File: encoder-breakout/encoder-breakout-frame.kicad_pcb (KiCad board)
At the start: 2 copper layers, 76 x 62.2 mm, 60 parts, among them J1 Conn_01x06_Female, U1 AEDR-8300

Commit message: Replace tooling holes with dual sided version
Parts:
- removed the REF** at (205.0, 112.0)
- removed the REF** at (205.0, 132.0)
- removed the REF** at (135.0, 142.0)
- added REF**: Tooling hole 4mm_4.04mm_paste, Jitter_Footprints:Tooling_hole_4mm_4.04mm_paste_dual_sided, F.Cu at (205.0, 112.0)
- added REF**: Tooling hole 4mm_4.04mm_paste, Jitter_Footprints:Tooling_hole_4mm_4.04mm_paste_dual_sided, F.Cu at (205.0, 132.0)
- added REF**: Tooling hole 4mm_4.04mm_paste, Jitter_Footprints:Tooling_hole_4mm_4.04mm_paste_dual_sided, F.Cu at (135.0, 142.0)
- REF**: value Tooling hole 4mm_4.04mm_paste -> Tooling hole 4mm_4.04mm_paste_dual_sided; footprint Jitter_Footprints:Tooling_hole_4mm_4.04mm_paste -> Jitter_Footprints:Tooling_hole_4mm_4.04mm_paste_dual_sided
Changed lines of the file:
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@@
-(kicad_pcb (version 20171130) (host pcbnew "(5.1.4-0-10_14)")
+(kicad_pcb (version 20171130) (host pcbnew 5.1.4-e60b266~84~ubuntu16.04.1)
   (general
     (thickness 1.6)
@@
       (outputformat 1)
       (mirror false)
-      (drillshape 1)
+      (drillshape 0)
       (scaleselection 1)
-      (outputdirectory ""))
+      (outputdirectory "gerber__76x63/"))
   )
   (net 0 "")
@@
     (add_net "Net-(R2-Pad2)")
   )
+  (module Jitter_Footprints:Tooling_hole_4mm_4.04mm_paste_dual_sided locked (layer F.Cu)
+    (at 205 112)
+    (fp_text reference REF** (at -4.8 -1.5) (layer F.SilkS) hide
+      (effects (font (size 1 1) (thickness 0.15)))
+    )
+    (fp_text value "Tooling hole 4mm_4.04mm_paste" (at 0 -3.2) (layer F.Fab) hide
+      (effects (font (size 1 1) (thickness 0.15)))
+    )
+    (pad "" np_thru_hole circle (at 0 0) (size 4 4) (drill 4) (layers *.Cu *.Paste *.Mask)
+      (solder_paste_margin 0.04))
+  )
+  (module Jitter_Footprints:Tooling_hole_4mm_4.04mm_paste_dual_sided locked (layer F.Cu)
+    (at 205 132)
+    (fp_text reference REF** (at -4.8 -1.5) (layer F.SilkS) hide
+      (effects (font (size 1 1) (thickness 0.15)))
+    )
+    (fp_text value "Tooling hole 4mm_4.04mm_paste" (at 0 -3.2) (layer F.Fab) hide
+      (effects (font (size 1 1) (thickness 0.15)))
+    )
+    (pad "" np_thru_hole circle (at 0 0) (size 4 4) (drill 4) (layers *.Cu *.Paste *.Mask)
+      (solder_paste_margin 0.04))
+  )
+  (module Jitter_Footprints:Tooling_hole_4mm_4.04mm_paste_dual_sided locked (layer F.Cu)
+    (at 135 142)
+    (fp_text reference REF** (at -4.8 -1.5) (layer F.SilkS) hide
+      (effects (font (size 1 1) (thickness 0.15)))
+    )
+    (fp_text value "Tooling hole 4mm_4.04mm_paste" (at 0 -3.2) (layer F.Fab) hide
+      (effects (font (size 1 1) (thickness 0.15)))
+    )
+    (pad "" np_thru_hole circle (at 0 0) (size 4 4) (drill 4) (layers *.Cu *.Paste *.Mask)
+      (solder_paste_margin 0.04))
+  )
+  (module Jitter_Footprints:Tooling_hole_4mm_4.04mm_paste_dual_sided locked (layer F.Cu)
+    (at 135 102)
+    (fp_text reference REF** (at -4.8 -1.5) (layer F.SilkS) hide
+      (effects (font (size 1 1) (thickness 0.15)))
+    )
+    (fp_text value "Tooling hole 4mm_4.04mm_paste_dual_sided" (at 0 -3.2) (layer F.Fab) hide
+      (effects (font (size 1 1) (thickness 0.15)))
+    )
+    (pad "" np_thru_hole circle (at 0 0) (size 4 4) (drill 4) (layers *.Cu *.Paste *.Mask)
+      (solder_paste_margin 0.04))
+  )
   (module Jitter_Footprints:MouseBite_3.7mmx2.2mm (layer F.Cu)
     (at 173 122.2 90)
@@
     (pad "" np_thru_hole circle (at 0.25 0.5 180) (size 0.5 0.5) (drill 0.5) (layers *.Cu *.Mask))
   )
-  (module Jitter_Footprints:Tooling_hole_4mm_4.04mm_paste locked (layer F.Cu)
-    (at 205 112)
-    (fp_text reference REF** (at -4.8 -1.5) (layer F.SilkS) hide
-      (effects (font (size 1 1) (thickness 0.15)))
-    )
-    (fp_text value "Tooling hole 4mm_4.04mm_paste" (at 0 -3.2) (layer F.Fab) hide
-      (effects (font (size 1 1) (thickness 0.15)))
-    )
-    (pad "" np_thru_hole circle (at 0 0) (size 4 4) (drill 4) (layers *.Cu *.Mask F.Paste)
-      (solder_paste_margin 0.04))
-  )
-  (module Jitter_Footprints:Tooling_hole_4mm_4.04mm_paste locked (layer F.Cu)
-    (at 205 132)
-    (fp_text reference REF** (at -4.8 -1.5) (layer F.SilkS) hide
-      (effects (font (size 1 1) (thickness 0.15)))
-    )
-    (fp_text value "Tooling hole 4mm_4.04mm_paste" (at 0 -3.2) (layer F.Fab) hide
-      (effects (font (size 1 1) (thickness 0.15)))
-    )
-    (pad "" np_thru_hole circle (at 0 0) (size 4 4) (drill 4) (layers *.Cu *.Mask F.Paste)
-      (solder_paste_margin 0.04))
-  )
-  (module Jitter_Footprints:Tooling_hole_4mm_4.04mm_paste locked (layer F.Cu)
-    (at 135 142)
-    (fp_text reference REF** (at -4.8 -1.5) (layer F.SilkS) hide
-      (effects (font (size 1 1) (thickness 0.15)))
-    )
-    (fp_text value "Tooling hole 4mm_4.04mm_paste" (at 0 -3.2) (layer F.Fab) hide
-      (effects (font (size 1 1) (thickness 0.15)))
-    )
-    (pad "" np_thru_hole circle (at 0 0) (size 4 4) (drill 4) (layers *.Cu *.Mask F.Paste)
-      (solder_paste_margin 0.04))
-  )
-  (module Jitter_Footprints:Tooling_hole_4mm_4.04mm_paste locked (layer F.Cu)
-    (at 135 102)
-    (fp_text reference REF** (at -4.8 -1.5) (layer F.SilkS) hide
-      (effects (font (size 1 1) (thickness 0.15)))
-    )
-    (fp_text value "Tooling hole 4mm_4.04mm_paste" (at 0 -3.2) (layer F.Fab) hide
-      (effects (font (size 1 1) (thickness 0.15)))
-    )
-    (pad "" np_thru_hole circle (at 0 0) (size 4 4) (drill 4) (layers *.Cu *.Mask F.Paste)
-      (solder_paste_margin 0.04))
-  )
-  (module Jitter_Footprints:MouseBite_3.7mmx2.2mm (layer F.Cu)
+  (module Jitter_Footprints:MouseBite_3.7mmx2.2mm (layer F.Cu)

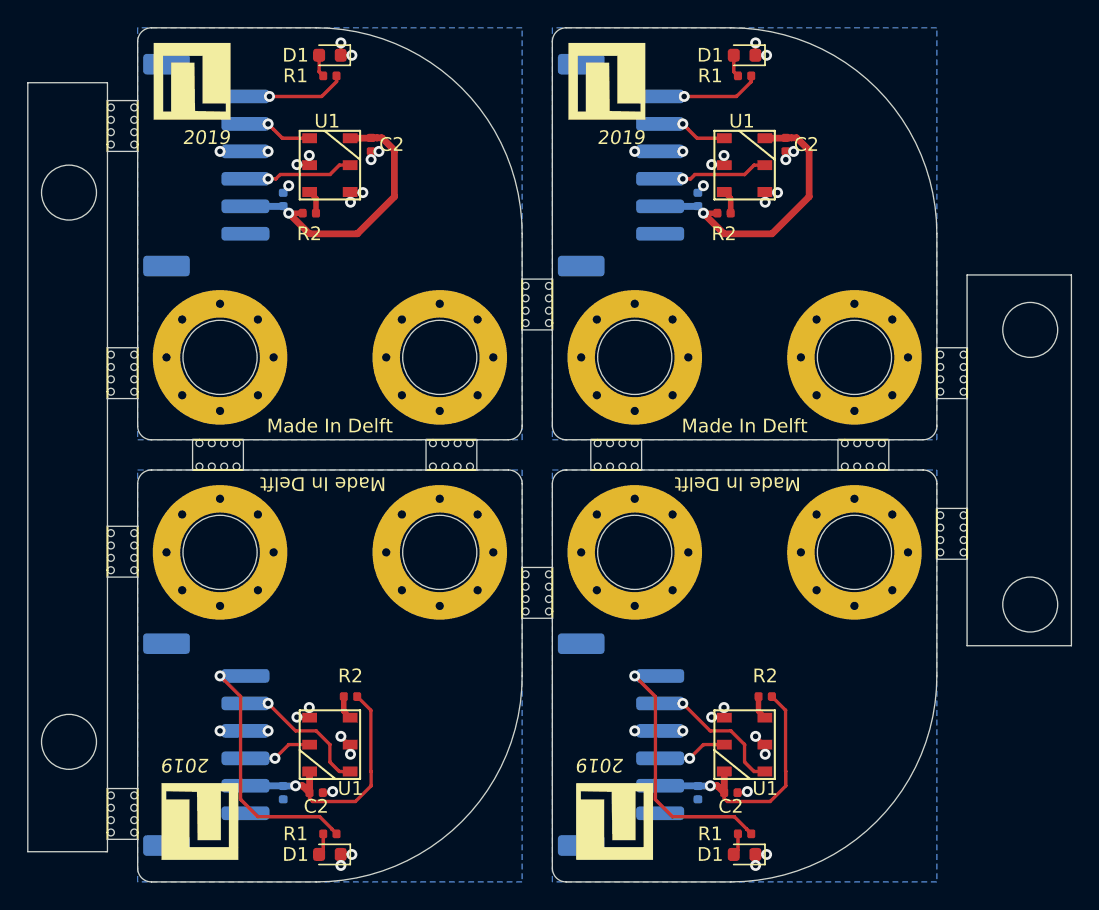
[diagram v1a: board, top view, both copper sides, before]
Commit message: Encoder breakout V2: sensor was rotated incorrectly!
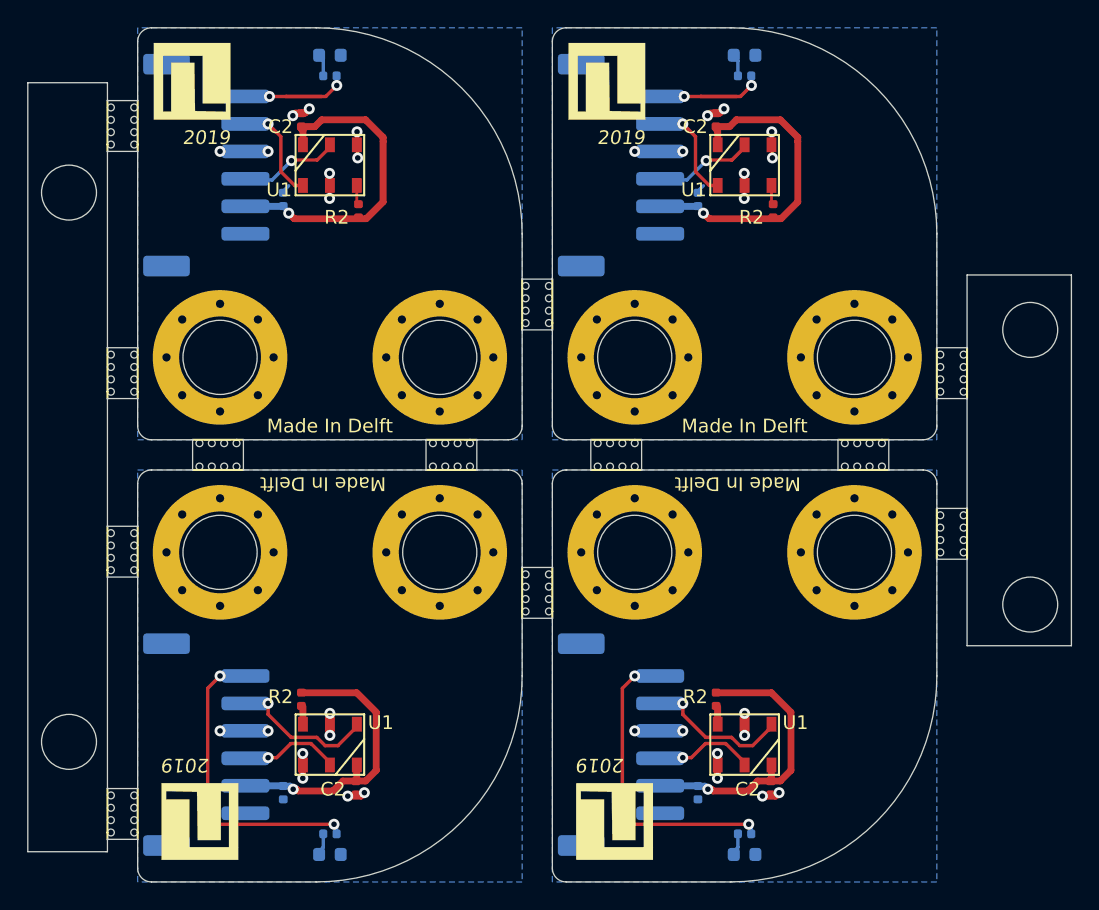
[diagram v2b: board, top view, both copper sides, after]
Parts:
- removed the C2 at (157.0, 98.5)
- removed the C2 at (153.0, 145.7)
- removed the C2 at (183.2, 145.7)
- removed the C2 at (187.2, 98.5)
- removed the R2 at (152.5, 103.5)
- removed the R2 at (155.5, 138.7)
- removed the R2 at (185.7, 138.7)
- removed the R2 at (182.7, 103.5)
- removed the REF** at (161.0, 122.2)
- removed the REF** at (144.0, 122.2)
- removed the REF** at (143.5, 94.0)
- removed the REF** at (160.0, 98.0)
- removed the REF** at (159.0, 144.2)
- removed the REF** at (145.0, 147.7)
- removed the REF** at (189.2, 144.2)
- removed the REF** at (175.2, 147.7)
- removed the REF** at (173.7, 94.0)
- removed the REF** at (190.2, 98.0)
- removed the REF** at (173.0, 122.2)
- removed the REF** at (191.0, 122.2)
- removed the REF** at (200.4, 128.7)
- added C2: 100nF, Capacitor_SMD:C_0402_1005Metric, F.Cu at (151.9, 96.7)
- added C2: 100nF, Capacitor_SMD:C_0402_1005Metric, F.Cu at (182.1, 96.7)
- added C2: 100nF, Capacitor_SMD:C_0402_1005Metric, F.Cu at (155.9, 145.3)
- added C2: 100nF, Capacitor_SMD:C_0402_1005Metric, F.Cu at (186.1, 145.3)
- added LOGO1: LOGO, Jitter_Logos:JitterLogo, F.Cu at (143.5, 94.0)
- added LOGO1: LOGO, Jitter_Logos:JitterLogo, F.Cu at (173.7, 94.0)
- added LOGO1: DNI, Jitter_Logos:JitterLogo, F.Cu at (145.0, 147.7)
- added LOGO1: DNI, Jitter_Logos:JitterLogo, F.Cu at (175.2, 147.7)
- added LOGO2: LOGO, Jitter_Logos:JitterLogo, B.Cu at (160.0, 98.0)
- added LOGO2: LOGO, Jitter_Logos:JitterLogo, B.Cu at (190.2, 98.0)
- added LOGO2: DNI, Jitter_Logos:JitterLogo, B.Cu at (159.0, 144.2)
- added LOGO2: DNI, Jitter_Logos:JitterLogo, B.Cu at (189.2, 144.2)
- added R2: 220, Resistor_SMD:R_0402_1005Metric, F.Cu at (156.1, 103.3)
- added R2: 220, Resistor_SMD:R_0402_1005Metric, F.Cu at (186.3, 103.3)
- added R2: 220, Resistor_SMD:R_0402_1005Metric, F.Cu at (151.9, 138.9)
- added R2: 220, Resistor_SMD:R_0402_1005Metric, F.Cu at (182.1, 138.9)
- added REF**: MouseBite_3.7mmx2.2mm, Jitter_Footprints:MouseBite_3.7mmx2.2mm, F.Cu at (198.2, 125.0)
- added REF**: MouseBite_3.7mmx2.2mm, Jitter_Footprints:MouseBite_3.7mmx2.2mm, F.Cu at (194.7, 120.0)
- added REF**: MouseBite_3.7mmx2.2mm, Jitter_Footprints:MouseBite_3.7mmx2.2mm, F.Cu at (176.7, 120.0)
- added REF**: MouseBite_3.7mmx2.2mm, Jitter_Footprints:MouseBite_3.7mmx2.2mm, F.Cu at (164.7, 120.0)
- added REF**: MouseBite_3.7mmx2.2mm, Jitter_Footprints:MouseBite_3.7mmx2.2mm, F.Cu at (147.7, 120.0)
- D1 (x4): value LED -> KPT-1608EC; moved to B.Cu
- H1 (x4), H2 (x4): value MountingHole_Pad -> 9774060482R
- J1 (x4): value Conn_01x06_Female -> Conn_01x06_MountingPin
- R1 (x4): moved to B.Cu
- turned U1 to 90 degrees (x2)
- turned U1 to 270 degrees (x2)
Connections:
- J1 pad MP: (no net) -> GND (x4)
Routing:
- net /STATUS_LED_3V3: track 46.8 -> 64.0 mm, vias 4 -> 8
- net +5V: track 79.3 -> 92.9 mm
- net /Ch_B: track 27.8 -> 33.0 mm
- net GND: track 25.3 -> 27.0 mm, vias 40 -> 32
- net Net-(R2-Pad2): track 6.93 -> 7.99 mm
- net Net-(D1-Pad2): track 6.50 -> 5.92 mm
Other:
- rule pad_to_mask_clearance: 0.051 -> 0.05
- rule solder_mask_min_width: 0.25 -> 0.15
